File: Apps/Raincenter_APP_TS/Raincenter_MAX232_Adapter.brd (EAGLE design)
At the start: 35 x 14.3 mm, 5 parts, among them IC101 MAX232ECSE

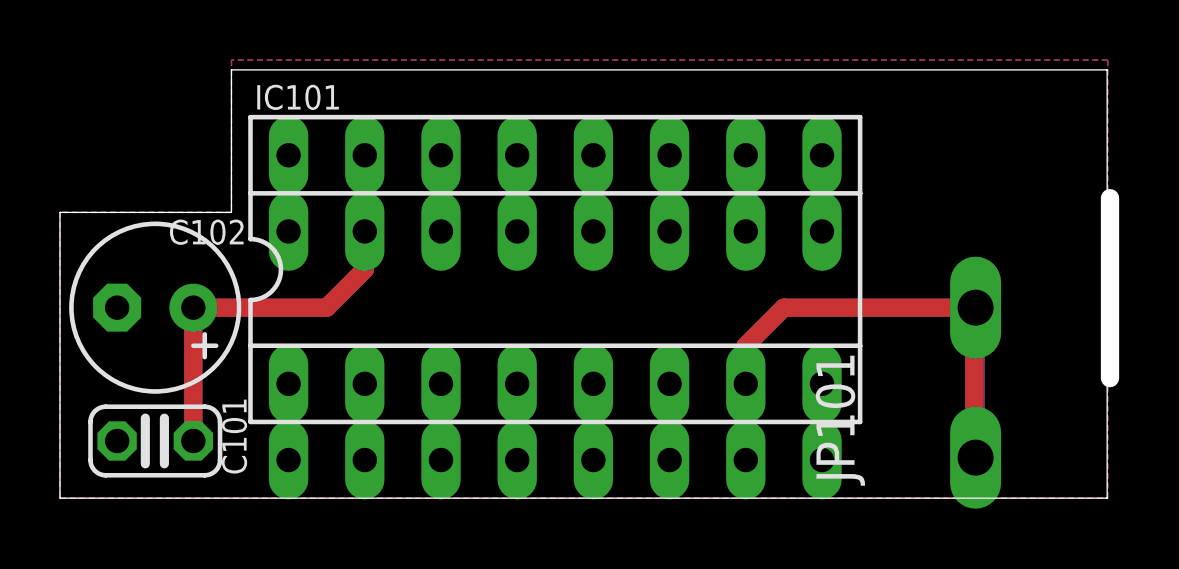
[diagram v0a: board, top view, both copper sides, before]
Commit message: Raincenter App: positioned tNames & bNames for production
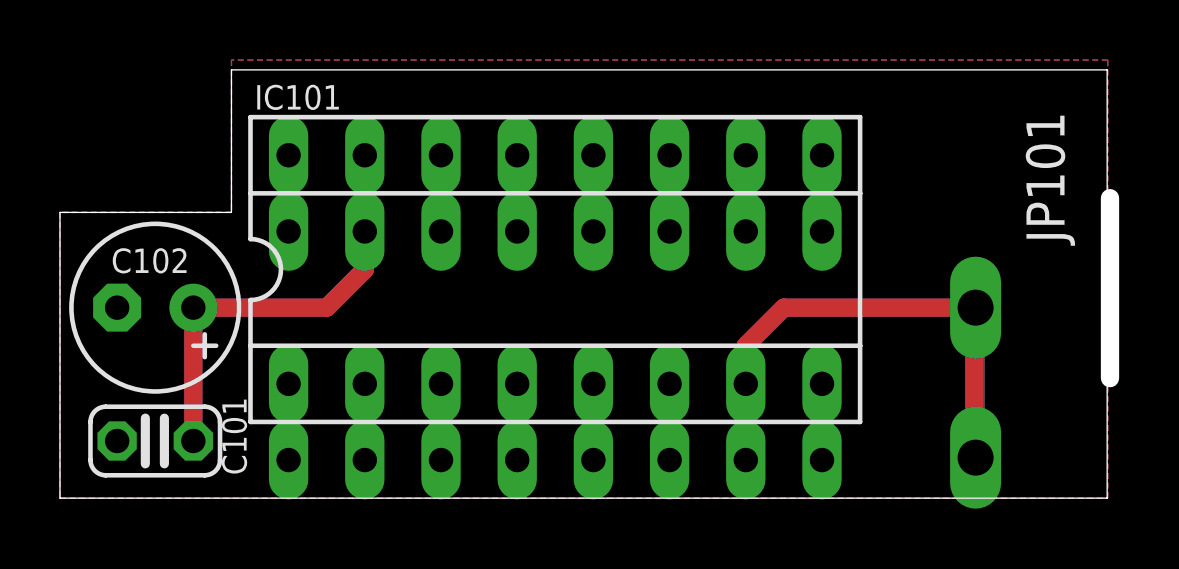
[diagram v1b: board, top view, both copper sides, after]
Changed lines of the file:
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@@
 <setting verticaltext="up"/>
 </settings>
-<grid distance="1" unitdist="mm" unit="mm" style="lines" multiple="1" display="yes" altdistance="12.5" altunitdist="mil" altunit="mil"/>
+<grid distance="25" unitdist="mil" unit="mil" style="lines" multiple="1" display="yes" altdistance="12.5" altunitdist="mil" altunit="mil"/>
 <layers>
 <layer number="1" name="Top" color="4" fill="1" visible="yes" active="yes"/>
@@
 <layer number="37" name="tTest" color="7" fill="1" visible="no" active="yes"/>
 <layer number="38" name="bTest" color="7" fill="1" visible="no" active="yes"/>
-<layer number="39" name="tKeepout" color="4" fill="11" visible="yes" active="yes"/>
-<layer number="40" name="bKeepout" color="1" fill="11" visible="yes" active="yes"/>
-<layer number="41" name="tRestrict" color="4" fill="10" visible="yes" active="yes"/>
-<layer number="42" name="bRestrict" color="1" fill="10" visible="yes" active="yes"/>
-<layer number="43" name="vRestrict" color="2" fill="10" visible="yes" active="yes"/>
+<layer number="39" name="tKeepout" color="4" fill="11" visible="no" active="yes"/>
+<layer number="40" name="bKeepout" color="1" fill="11" visible="no" active="yes"/>
+<layer number="41" name="tRestrict" color="4" fill="10" visible="no" active="yes"/>
+<layer number="42" name="bRestrict" color="1" fill="10" visible="no" active="yes"/>
+<layer number="43" name="vRestrict" color="2" fill="10" visible="no" active="yes"/>
 <layer number="44" name="Drills" color="7" fill="1" visible="no" active="yes"/>
 <layer number="45" name="Holes" color="7" fill="1" visible="no" active="yes"/>
-<layer number="46" name="Milling" color="3" fill="1" visible="yes" active="yes"/>
+<layer number="46" name="Milling" color="3" fill="1" visible="no" active="yes"/>
 <layer number="47" name="Measures" color="7" fill="1" visible="no" active="yes"/>
-<layer number="48" name="Document" color="7" fill="1" visible="yes" active="yes"/>
-<layer number="49" name="Reference" color="7" fill="1" visible="yes" active="yes"/>
+<layer number="48" name="Document" color="7" fill="1" visible="no" active="yes"/>
+<layer number="49" name="Reference" color="7" fill="1" visible="no" active="yes"/>
 <layer number="50" name="dxf" color="7" fill="1" visible="no" active="no"/>
-<layer number="51" name="tDocu" color="7" fill="1" visible="yes" active="yes"/>
-<layer number="52" name="bDocu" color="7" fill="1" visible="yes" active="yes"/>
+<layer number="51" name="tDocu" color="7" fill="1" visible="no" active="yes"/>
+<layer number="52" name="bDocu" color="7" fill="1" visible="no" active="yes"/>
 <layer number="53" name="tGND_GNDA" color="7" fill="9" visible="no" active="no"/>
 <layer number="54" name="bGND_GNDA" color="1" fill="9" visible="no" active="no"/>
@@
 <layer number="97" name="Info" color="7" fill="1" visible="no" active="no"/>
 <layer number="98" name="Guide" color="6" fill="1" visible="no" active="no"/>
-<layer number="100" name="Muster" color="7" fill="1" visible="yes" active="yes"/>
-<layer number="101" name="Patch_Top" color="7" fill="1" visible="yes" active="yes"/>
-<layer number="102" name="bot_pads" color="7" fill="1" visible="yes" active="yes"/>
-<layer number="103" name="Stiffner" color="7" fill="1" visible="yes" active="yes"/>
-<layer number="104" name="S_DOKU" color="7" fill="1" visible="yes" active="yes"/>
-<layer number="105" name="Beschreib" color="7" fill="1" visible="yes" active="yes"/>
-<layer number="106" name="BGA-Top" color="7" fill="1" visible="yes" active="yes"/>
-<layer number="107" name="BD-Top" color="7" fill="1" visible="yes" active="yes"/>
-<layer number="108" name="tBridges" color="7" fill="1" visible="yes" active="yes"/>
-<layer number="109" name="tBPL" color="7" fill="1" visible="yes" active="yes"/>
-<layer number="110" name="bBPL" color="7" fill="1" visible="yes" active="yes"/>
-<layer number="111" name="MPL" color="7" fill="1" visible="yes" active="yes"/>
-<layer number="112" name="tSilk" color="7" fill="1" visible="yes" active="yes"/>
-<layer number="116" name="Patch_BOT" color="7" fill="1" visible="yes" active="yes"/>
-<layer number="121" name="sName" color="7" fill="1" visible="yes" active="yes"/>
-<layer number="122" name="_bPlace" color="7" fill="1" visible="yes" active="yes"/>
-<layer number="125" name="_tNames" color="7" fill="1" visible="yes" active="yes"/>
-<layer number="126" name="_bNames" color="7" fill="1" visible="yes" active="yes"/>
-<layer number="127" name="_tValues" color="7" fill="1" visible="yes" active="yes"/>
-<layer number="128" name="_bValues" color="7" fill="1" visible="yes" active="yes"/>
-<layer number="144" name="Drill_legend" color="7" fill="1" visible="yes" active="yes"/>
-<layer number="151" name="HeatSink" color="7" fill="1" visible="yes" active="yes"/>
-<layer number="152" name="_bDocu" color="7" fill="1" visible="yes" active="yes"/>
-<layer number="199" name="Contour" color="7" fill="1" visible="yes" active="yes"/>
-<layer number="200" name="200bmp" color="7" fill="1" visible="yes" active="yes"/>
-<layer number="201" name="201bmp" color="7" fill="1" visible="yes" active="yes"/>
-<layer number="202" name="202bmp" color="7" fill="1" visible="yes" active="yes"/>
-<layer number="203" name="203bmp" color="7" fill="1" visible="yes" active="yes"/>
-<layer number="204" name="204bmp" color="7" fill="1" visible="yes" active="yes"/>
-<layer number="205" name="205bmp" color="7" fill="1" visible="yes" active="yes"/>
-<layer number="231" name="Eagle3D_PG1" color="14" fill="1" visible="yes" active="yes"/>
-<layer number="248" name="Housing" color="7" fill="1" visible="yes" active="yes"/>
-<layer number="249" name="Edge" color="7" fill="1" visible="yes" active="yes"/>
-<layer number="250" name="Descript" color="7" fill="1" visible="yes" active="yes"/>
-<layer number="251" name="SMDround" color="7" fill="1" visible="yes" active="yes"/>
-<layer number="254" name="OrgLBR" color="7" fill="1" visible="yes" active="yes"/>
 </layers>
 <board>
@@
 </variantdefs>
 <classes>
-<class number="0" name="default" width="0" drill="0">
+<class number="0" name="default" width="0.6096" drill="0">
 </class>
 </classes>
@@
 <elements>
 <element name="IC101" library="ic-package" package="SOCKET-16" value="MAX232ECSE" x="16.51" y="7.62" smashed="yes">
-<attribute name="REICHELT" value="GS 16P" x="16.51" y="7.62" size="1.778" layer="27" display="off"/>
+<attribute name="OC_REICHELT" value="GS 16P" x="16.51" y="7.62" size="1.778" layer="27" display="off"/>
 <attribute name="VALUE" x="28.575" y="2.54" size="1.27" layer="27" ratio="10" rot="R90"/>
 <attribute name="NAME" x="6.477" y="12.954" size="0.8128" layer="25" ratio="10"/>
 </element>
 <element name="JP102" library="ic-package" package="SOCKET-16" value="Raincenter" x="16.51" y="5.08" smashed="yes" rot="MR180">
-<attribute name="REICHELT" value="AR 16" x="16.51" y="5.08" size="1.778" layer="28" rot="MR180" display="off"/>
+<attribute name="OC_REICHELT" value="AR 16" x="16.51" y="5.08" size="1.778" layer="28" rot="MR180" display="off"/>
 <attribute name="MF" value="ASSMANN" x="16.51" y="5.08" size="1.778" layer="28" rot="MR180" display="off"/>
 <attribute name="MPN" value="AR-16-ST/T" x="16.51" y="5.08" size="1.778" layer="28" rot="MR180" display="off"/>
 <attribute name="VALUE" x="27.305" y="0" size="1.27" layer="28" ratio="10" rot="MR90"/>
-<attribute name="NAME" x="4.8895" y="5.1435" size="0.8128" layer="26" ratio="10" rot="MR180"/>
+<attribute name="NAME" x="14.8895" y="6.1435" size="0.8128" layer="26" ratio="10" rot="MR180"/>
 </element>
 <element name="C102" library="rcl" package="E2,5-6" value="1µF/100V" x="3.175" y="6.35" smashed="yes" rot="R180">
-<attribute name="REICHELT" value="RAD 105 1,0/100" x="3.175" y="6.35" size="1.778" layer="27" rot="R180" display="off"/>
-<attribute name="NAME" x="6.223" y="9.271" size="0.8128" layer="25" ratio="10" rot="R180"/>
+<attribute name="OC_REICHELT" value="RAD 105 1,0/100" x="3.175" y="6.35" size="1.778" layer="27" rot="R180" display="off"/>
+<attribute name="NAME" x="4.318" y="8.3185" size="0.8128" layer="25" ratio="10" rot="R180"/>
 <attribute name="VALUE" x="0.508" y="9.017" size="1.27" layer="27" ratio="10" rot="R180"/>
 </element>
 <element name="C101" library="rcl" package="C025-024X044" value="100nF/50V" x="3.175" y="1.905" smashed="yes" rot="R180">
 <attribute name="MN" value="Murata" x="3.175" y="1.905" size="1.778" layer="27" rot="R180" display="off"/>
-<attribute name="REICHELT" value="X7R-2,5 100N" x="3.175" y="1.905" size="1.778" layer="27" rot="R180" display="off"/>
+<attribute name="OC_REICHELT" value="X7R-2,5 100N" x="3.175" y="1.905" size="1.778" layer="27" rot="R180" display="off"/>
 <attribute name="NAME" x="6.223" y="0.762" size="0.8128" layer="25" ratio="10" rot="R90"/>
 <attribute name="VALUE" x="4.953" y="4.572" size="1.27" layer="27" ratio="10" rot="R180"/>
 </element>
-<element name="JP101" library="Klemmen" package="255-401-5" value="256-101" x="33.02" y="6.35">
+<element name="JP101" library="Klemmen" package="255-401-5" value="256-101" x="33.02" y="6.35" smashed="yes">
 <attribute name="MN" value="WAGO" x="33.02" y="6.35" size="1.778" layer="27" display="off"/>
 <attribute name="CONRAD" value="1x730366 + 1x730378" x="33.02" y="6.35" size="1.778" layer="27" display="off"/>
 <attribute name="MPN" value="1x 256-101 + 1x 256-100" x="33.02" y="6.35" size="1.778" layer="27" display="off"/>
+<attribute name="NAME" x="33.485" y="8.495" size="1.27" layer="25" rot="R90"/>
+<attribute name="VALUE" x="36.92" y="0.6" size="1.27" layer="27" rot="R90"/>
 </element>
 </elements>
